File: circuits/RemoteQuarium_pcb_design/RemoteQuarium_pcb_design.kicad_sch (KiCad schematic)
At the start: 37 parts, among them J1 Power_terminal, J10 LCD_pins, J11 Feeder_servo_pins, J12 ESP_pins, J13 PH_sensor_sockets, J14 Ph_sesnor-pins, J15 Power & D3-D4, J16 Reset_button_terminal, J2 ESP left side sockets, J3 ESP right side sockets, J4 Relay_terminal, J5 SREG_pins, J6 Temp_sensor_terminal, J7 Water_sensor_terminal, J8 Light_sensor_terminal, J9 MUX_pins, Q1 BC547, Q2 BC547, Q3 BC547, Q4 BC547, Q5 BC547, U2 74HC595, U3 CD4052B

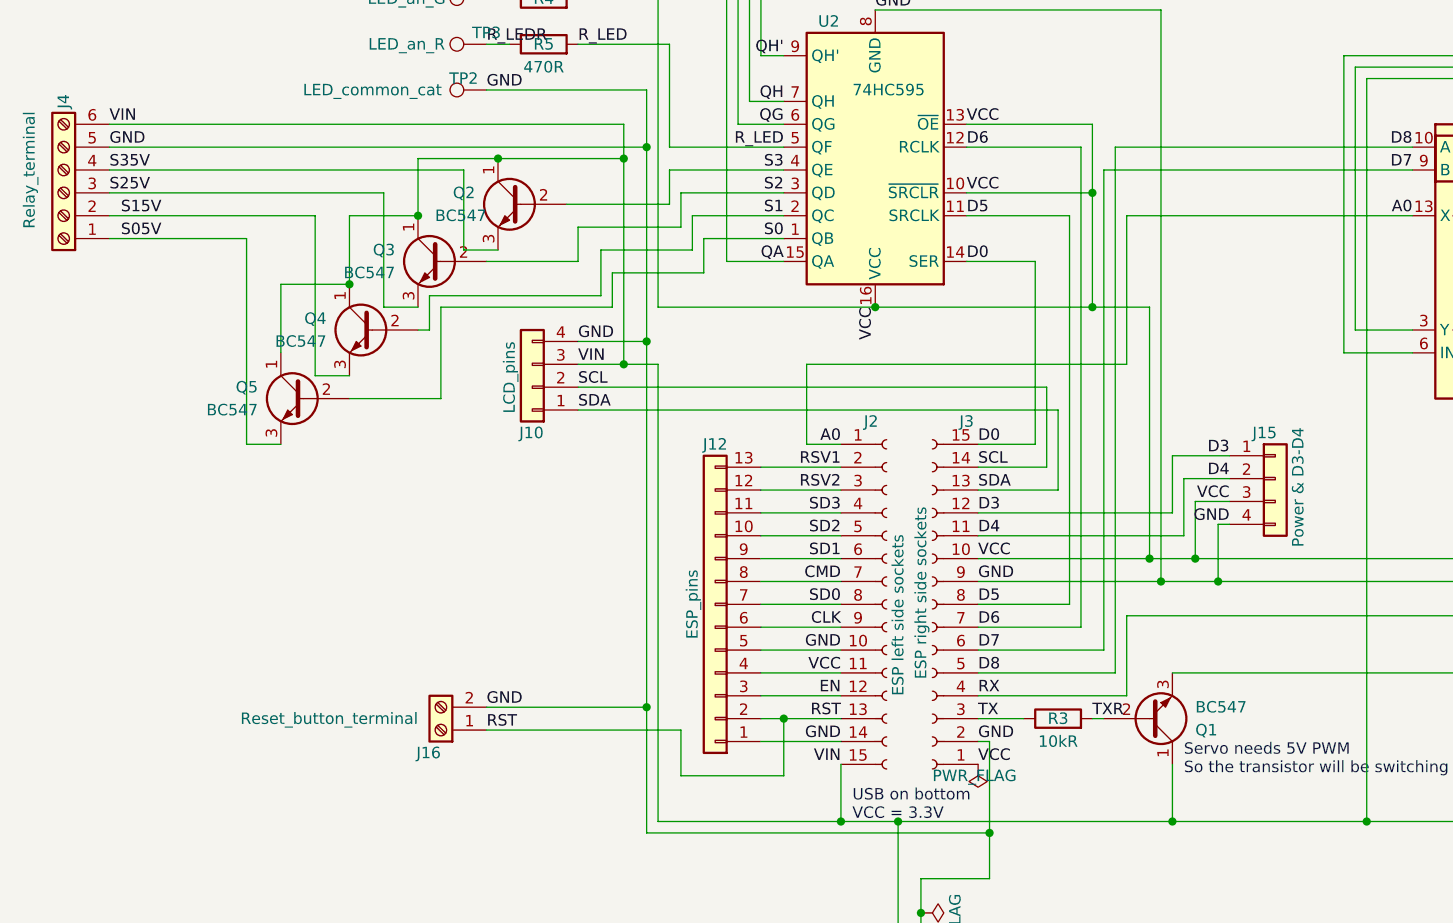
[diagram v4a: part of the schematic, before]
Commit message: Minor changes to the strings and to notification are working, also made a working dev build
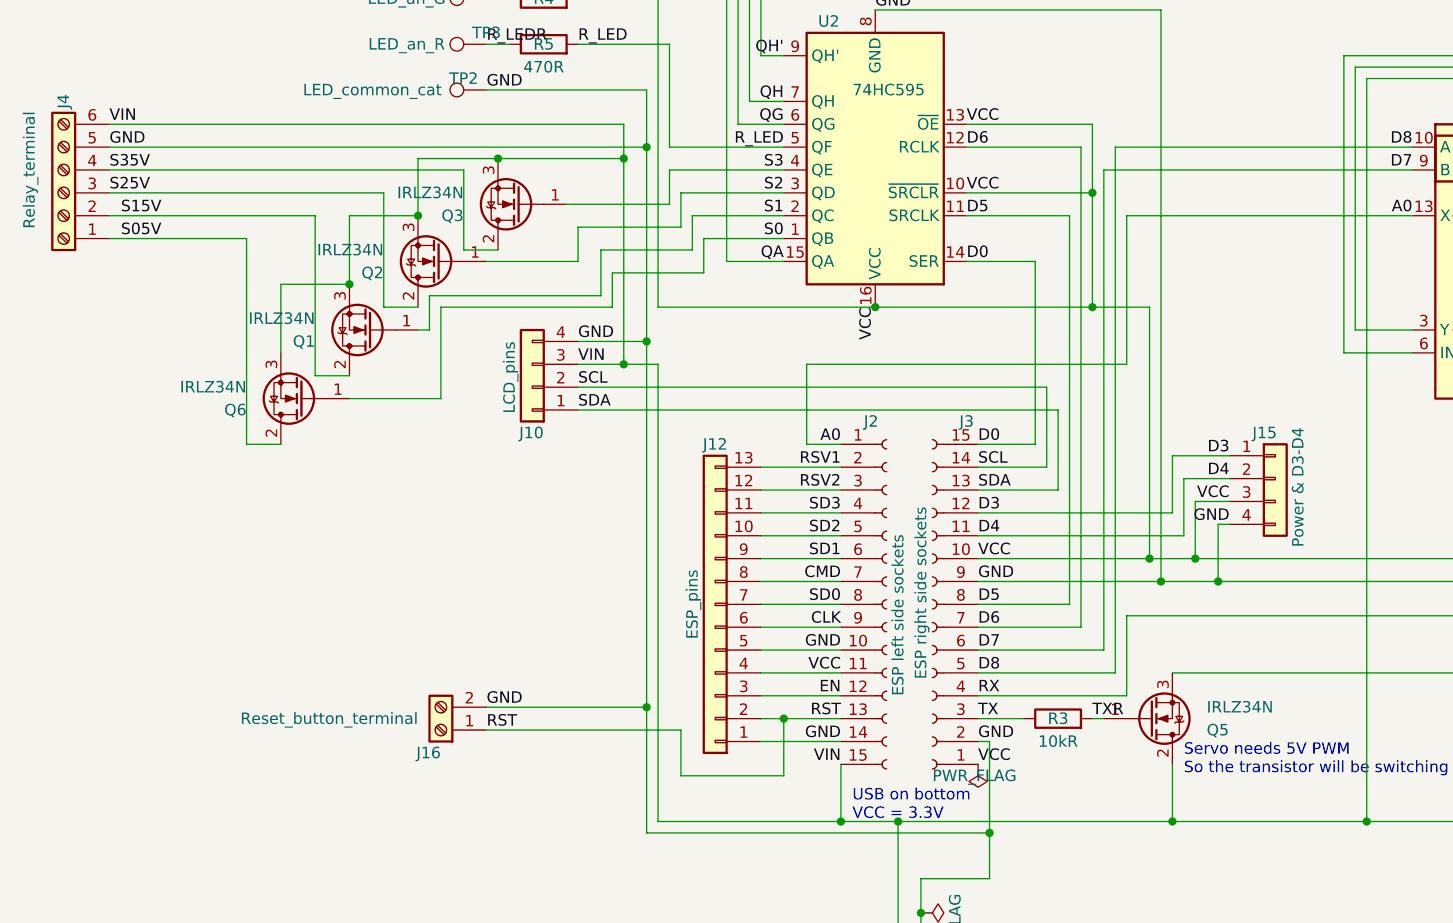
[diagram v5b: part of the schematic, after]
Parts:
- removed Q1, Q2, Q3, Q4, Q5: BC547, Package_TO_SOT_THT:TO-92_Inline, symbol Transistor_BJT:BC547
- added Q1, Q2, Q3, Q5, Q6: IRLZ34N, Package_TO_SOT_THT:TO-220-3_Vertical, symbol Transistor_FET:IRLZ34N
- J16: footprint TerminalBlock_Phoenix:TerminalBlock_Phoenix_MPT-0,5-2-2.54_1x02_P2.54mm_Horizontal -> NXW:NXW-02P
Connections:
- net S0: now also Q6.1 (G)
- net S05V: now also Q6.2 (D)
- net S1: now also Q1.1 (G)
- net S15V: now also Q1.2 (D)
- net S2: now also Q2.1 (G)
- net S25V: now also Q2.2 (D)
- net S3: now also Q3.1 (G)
- net S35V: now also Q3.2 (D)
- net TX5V: now also Q5.3 (S)
- net TXR: now also Q5.1 (G)
- net VIN: now also Q1.3 (S), Q2.3 (S), Q3.3 (S), Q5.2 (D), Q6.3 (S)

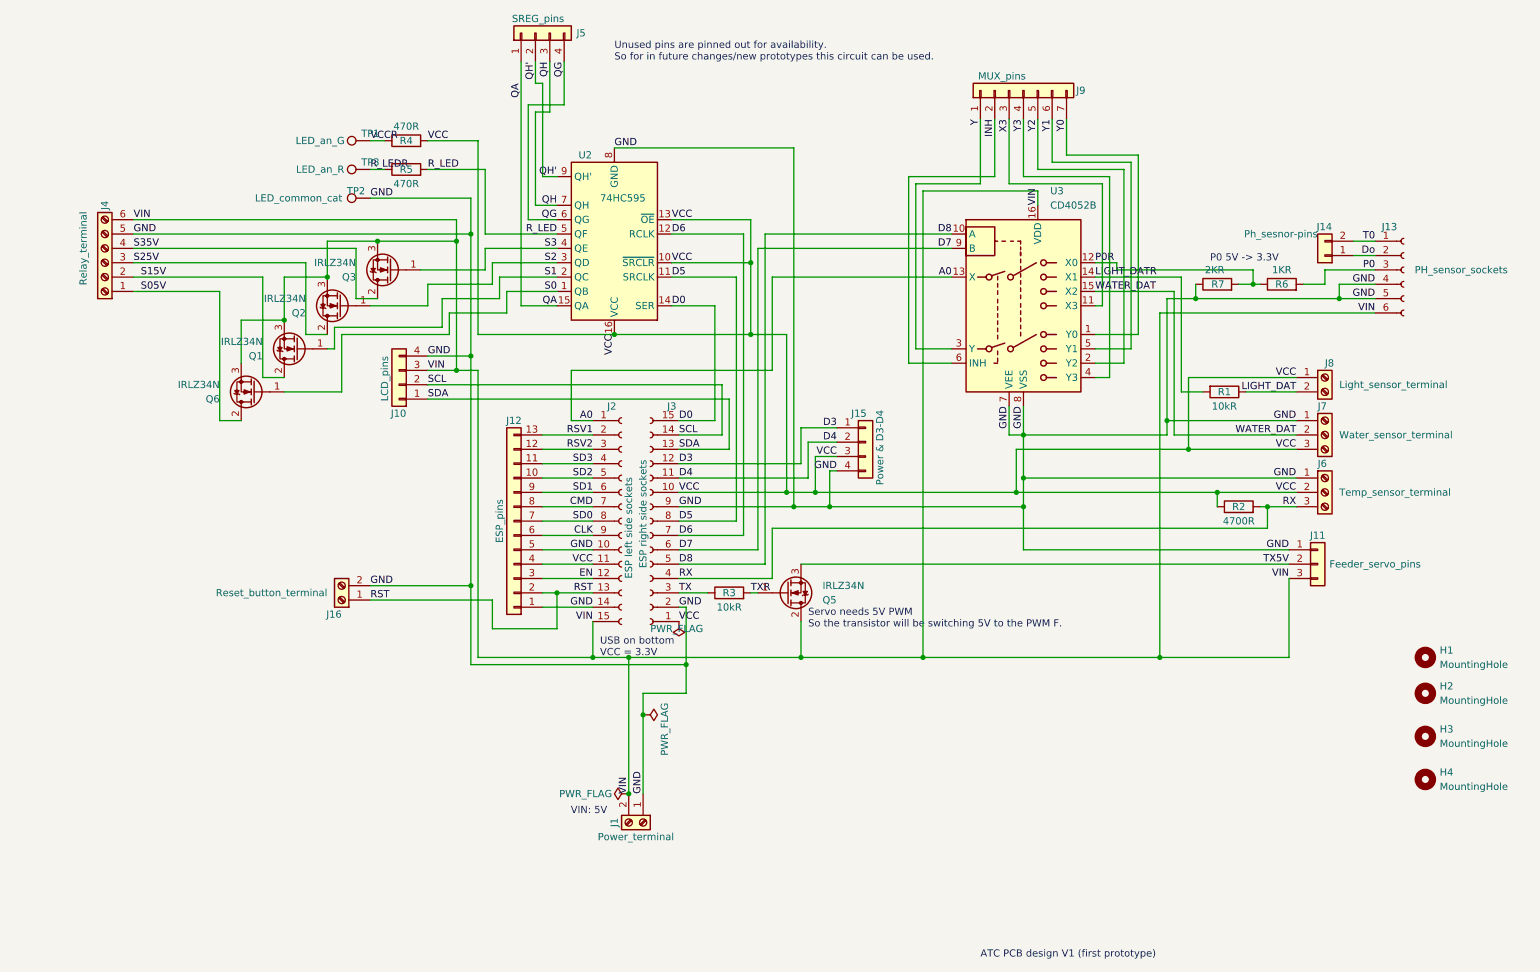
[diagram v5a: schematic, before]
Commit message: Notifications are working, also fixed up the circuit a little. Added all notifications to switch in main
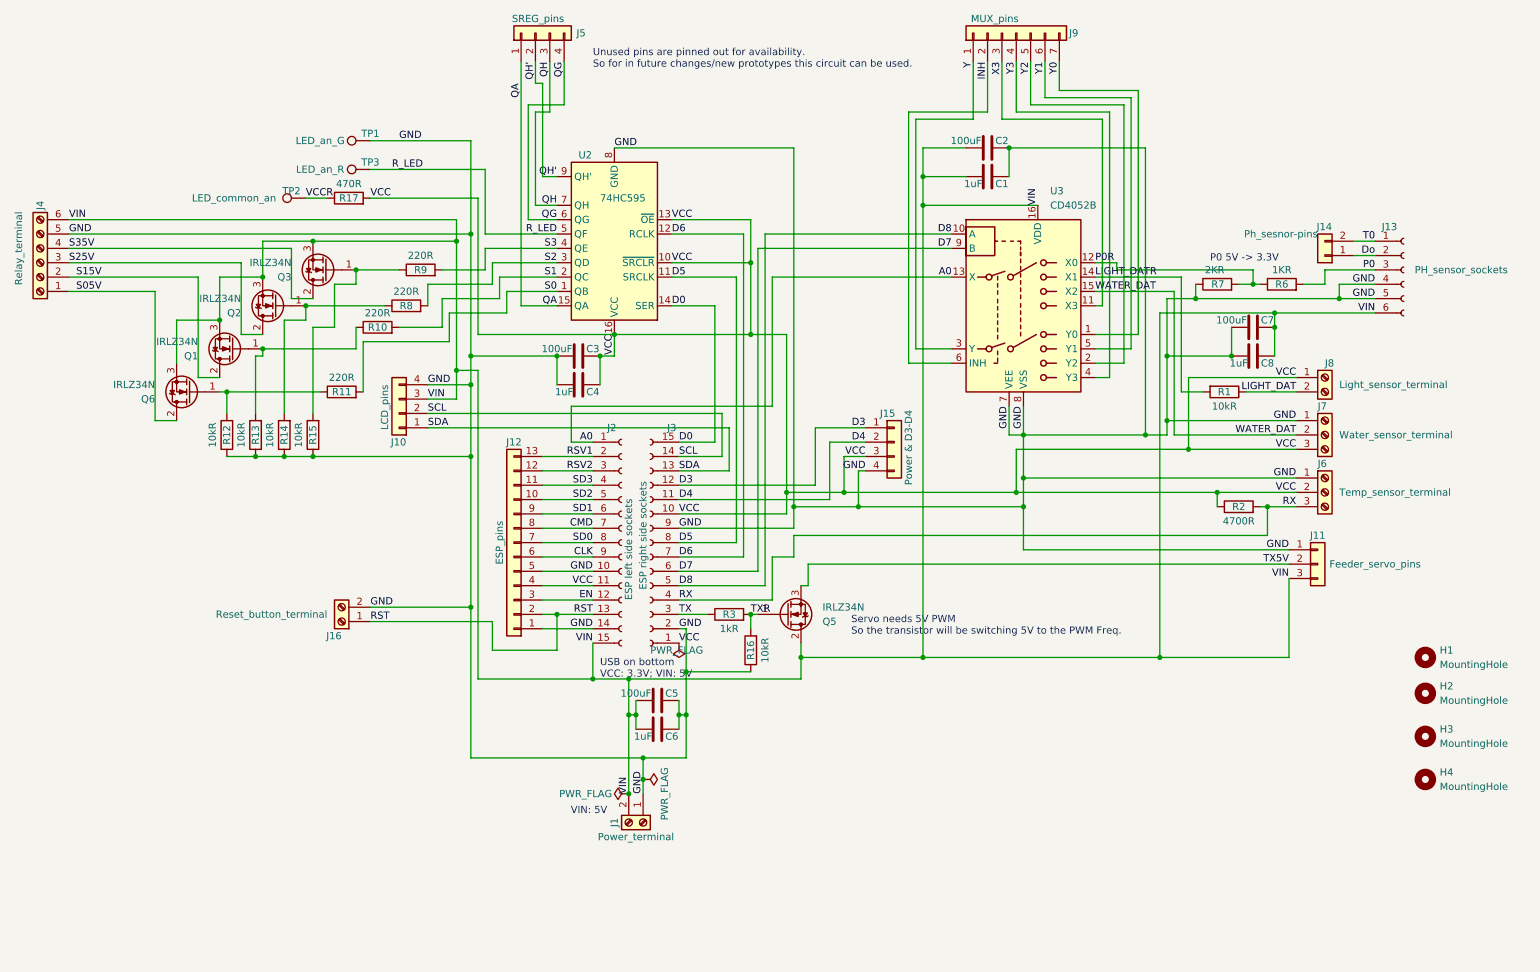
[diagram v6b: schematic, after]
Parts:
- removed R4, R5: 470R, Resistor_THT:R_Axial_DIN0204_L3.6mm_D1.6mm_P5.08mm_Horizontal, symbol Device:R
- added C1, C4, C6, C8: 1uF, Capacitor_THT:CP_Radial_D4.0mm_P1.50mm, symbol Device:C
- added C2, C3, C5, C7: 100uF, Capacitor_THT:CP_Radial_D6.3mm_P2.50mm, symbol Device:C
- added R10, R11, R8, R9: 220R, Resistor_THT:R_Axial_DIN0207_L6.3mm_D2.5mm_P7.62mm_Horizontal, symbol Device:R
- added R12, R13, R14, R15, R16: 10kR, Resistor_THT:R_Axial_DIN0207_L6.3mm_D2.5mm_P7.62mm_Horizontal, symbol Device:R
- added R17: 470R, Resistor_THT:R_Axial_DIN0207_L6.3mm_D2.5mm_P7.62mm_Horizontal, symbol Device:R
- R1, R2, R6, R7: footprint Resistor_THT:R_Axial_DIN0204_L3.6mm_D1.6mm_P5.08mm_Horizontal -> Resistor_THT:R_Axial_DIN0207_L6.3mm_D2.5mm_P7.62mm_Horizontal
- R3: value 10kR -> 1kR; footprint Resistor_THT:R_Axial_DIN0204_L3.6mm_D1.6mm_P5.08mm_Horizontal -> Resistor_THT:R_Axial_DIN0207_L6.3mm_D2.5mm_P7.62mm_Horizontal
- TP2: value LED_common_cat -> LED_common_an
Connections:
- net R_LEDR is gone; now on net R_LED: TP3.1
- net GND: now also TP1.1, C1.2, C2.2, C3.1, C4.1, C5.2, C6.2, C7.1, C8.1, R12.1, R13.1, R14.1, R15.1, R16.1; no longer TP2.1
- net S0: now also R11.2; no longer Q6.1 (G)
- net S1: now also R10.2; no longer Q1.1 (G)
- net S2: now also R8.2; no longer Q2.1 (G)
- net S3: now also R9.2; no longer Q3.1 (G)
- net TXR: now also R16.2
- net VCC: now also C3.2, C4.2, R17.2
- net VCCR: now also TP2.1, R17.1; no longer TP1.1
- net VIN: now also C1.1, C2.1, C5.1, C6.1, C7.2, C8.2
- new net: Q6.1 (G), R11.1, R12.2
- new net: Q2.1 (G), R14.2, R8.1
- new net: Q1.1 (G), R10.1, R13.2
- new net: Q3.1 (G), R15.2, R9.1
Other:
- note added: "Servo needs 5V PWM So the transistor will be switching 5V to the PWM Freq."
- note added: "USB on bottom VCC: 3.3V; VIN: 5V"
- note removed: "ATC PCB design V1 (first prototype)"
- note removed: "Servo needs 5V PWM So the transistor will be switching 5V to the PWM F."
- note removed: "USB on bottom VCC = 3.3V"
- moved on the sheet: J10, J12, J15, J16, J2, J3, J4, J9, Q1, Q2, Q3, Q5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

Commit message: Modified DB so user have an ID now. Also fixed (hopefully need to double check) statistics data fill is scaled with sample period. Added factory reset function which is working. All other should work as usual. Removed -1 hour offset of samples timestamp bc now it was good xdd
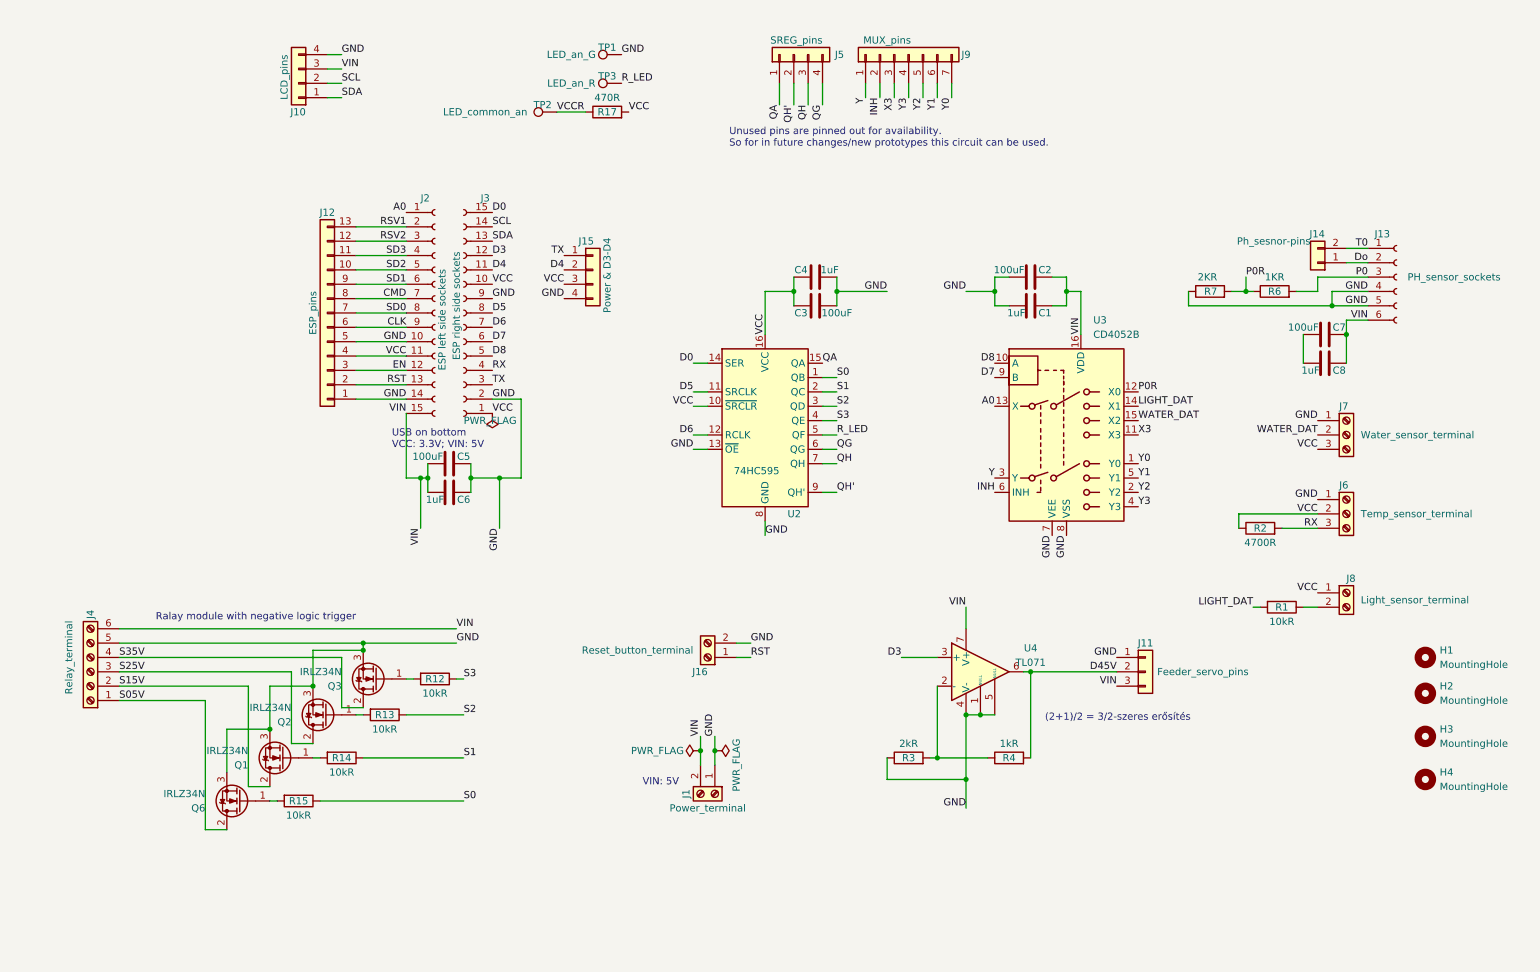
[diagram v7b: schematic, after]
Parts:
- removed Q5: IRLZ34N, Package_TO_SOT_THT:TO-220-3_Vertical, symbol Transistor_FET:IRLZ34N
- removed R10, R11, R8, R9: 220R, Resistor_THT:R_Axial_DIN0207_L6.3mm_D2.5mm_P7.62mm_Horizontal, symbol Device:R
- removed R16: 10kR, Resistor_THT:R_Axial_DIN0207_L6.3mm_D2.5mm_P7.62mm_Horizontal, symbol Device:R
- added R4: 1kR, symbol Device:R
- added U4: TL071, symbol Amplifier_Operational:TL071
- R3: value 1kR -> 2kR; footprint Resistor_THT:R_Axial_DIN0207_L6.3mm_D2.5mm_P7.62mm_Horizontal -> (none)
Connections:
- net LIGHT_DATR is gone; now on net LIGHT_DAT: R1.2, U3.14 (X1)
- net D3: now also U4.3 (+); no longer J15.1 (Pin_1)
- net GND: now also C1.1, C2.1, Q1.3 (S), Q2.3 (S), Q3.3 (S), Q6.3 (S), R3.1, U2.13 (~{OE}), U4.1 (NULL), U4.4 (V-), U4.5 (NULL); no longer C1.2, C2.2, C7.1, C8.1, R12.1, R13.1, R14.1, R15.1
- net LIGHT_DAT: no longer J8.2 (Pin_2), R1.1
- net S0: now also R15.1
- net S1: now also R14.1
- net S2: now also R13.1
- net S3: now also R12.1
- net TX: now also J15.1 (Pin_1); no longer R3.1
- net VCC: no longer U2.13 (~{OE})
- net VIN: now also C1.2, C2.2, U4.7 (V+); no longer C1.1, C2.1, Q1.3 (S), Q2.3 (S), Q3.3 (S), Q6.3 (S)
- net at R12.2: now also Q3.1 (G); no longer Q6.1 (G)
- net at R14.2: now also Q1.1 (G); no longer Q2.1 (G)
- net at R13.2: now also Q2.1 (G); no longer Q1.1 (G)
- net at R15.2: now also Q6.1 (G); no longer Q3.1 (G)
- net TX5V renamed D45V
- net D45V: now also R4.2, U4.6
- net TXR: no longer names the net of R3.2
- net TXR: now also R4.1, U4.2 (-)
- new net: J8.2 (Pin_2), R1.1
- new net: C7.1, C8.1
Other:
- note added: "(2+1)/2 = 3/2-szeres erősítés"
- note added: "Ralay module with negative logic trigger"
- note removed: "P0 5V -> 3.3V"
- note removed: "Servo needs 5V PWM So the transistor will be switching 5V to the PWM Freq."
- moved on the sheet: C1, C2, C3, C4, C5, C6, C7, C8, J1, J10, J11, J12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

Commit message: Added users and systems page (basic) also modified circuit with decoupling capacitors
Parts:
- removed C7: 100uF, Capacitor_THT:CP_Radial_D6.3mm_P2.50mm, symbol Device:C
- removed C8: 1uF, Capacitor_THT:CP_Radial_D4.0mm_P1.50mm, symbol Device:C
- added R10, R5, R8, R9: 10kR, Resistor_THT:R_Axial_DIN0207_L6.3mm_D2.5mm_P7.62mm_Horizontal, symbol Device:R
- C1, C4, C6: value 1uF -> 0.1uF
- C2, C3, C5: value 100uF -> 10uF
- R12, R13, R14, R15: value 10kR -> 4.7kR
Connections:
- net GND: now also R10.2, R5.2, R8.2, R9.2
- net S1: now also R10.1, R9.1
- net S2: now also R8.1
- net S3: now also R5.1
